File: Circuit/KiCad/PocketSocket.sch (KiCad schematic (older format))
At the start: 0 parts

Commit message: add PowerInput
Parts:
- added C?: 0.1u, symbol C
- added C? (x2): 1u, symbol C
- added P?: CONN_02X25, symbol CONN_02X25
- added P?: I2C_LCD, symbol CONN_01X04
- added U?: CY8CKIT-059_Target, symbol CY8CKIT-059_Target
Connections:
- new net +5V: C?.1, C?.1, C?.2, P?.1 (P1), U?.26 (VDD), U?.52 (VDDIO)
- new net GND: C?.1, C?.2, C?.2, P?.4 (P4), U?.1 (GND), U?.25 (GND), U?.51 (GND)
- new net SCL: P?.2 (P2), U?.42 (P12[0]_I2C_SCL)
- new net SDA: P?.3 (P3), U?.41 (P12[1]_I2C_SDA)
- no-connect marks 0 -> 12

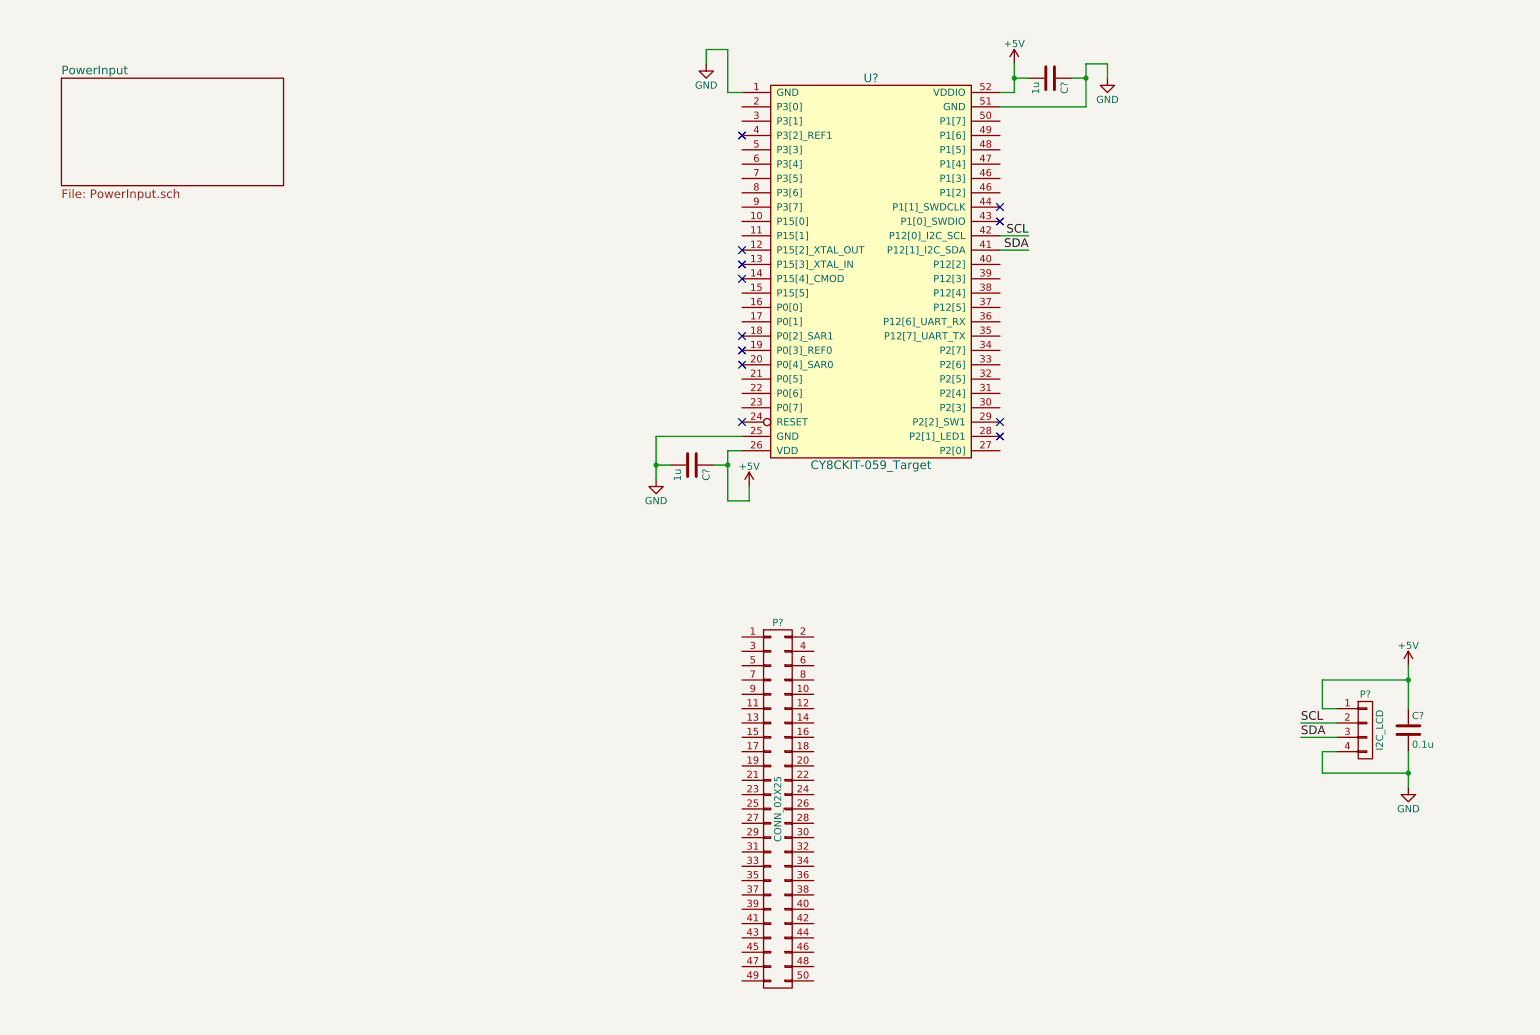
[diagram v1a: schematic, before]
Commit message: add LED driver
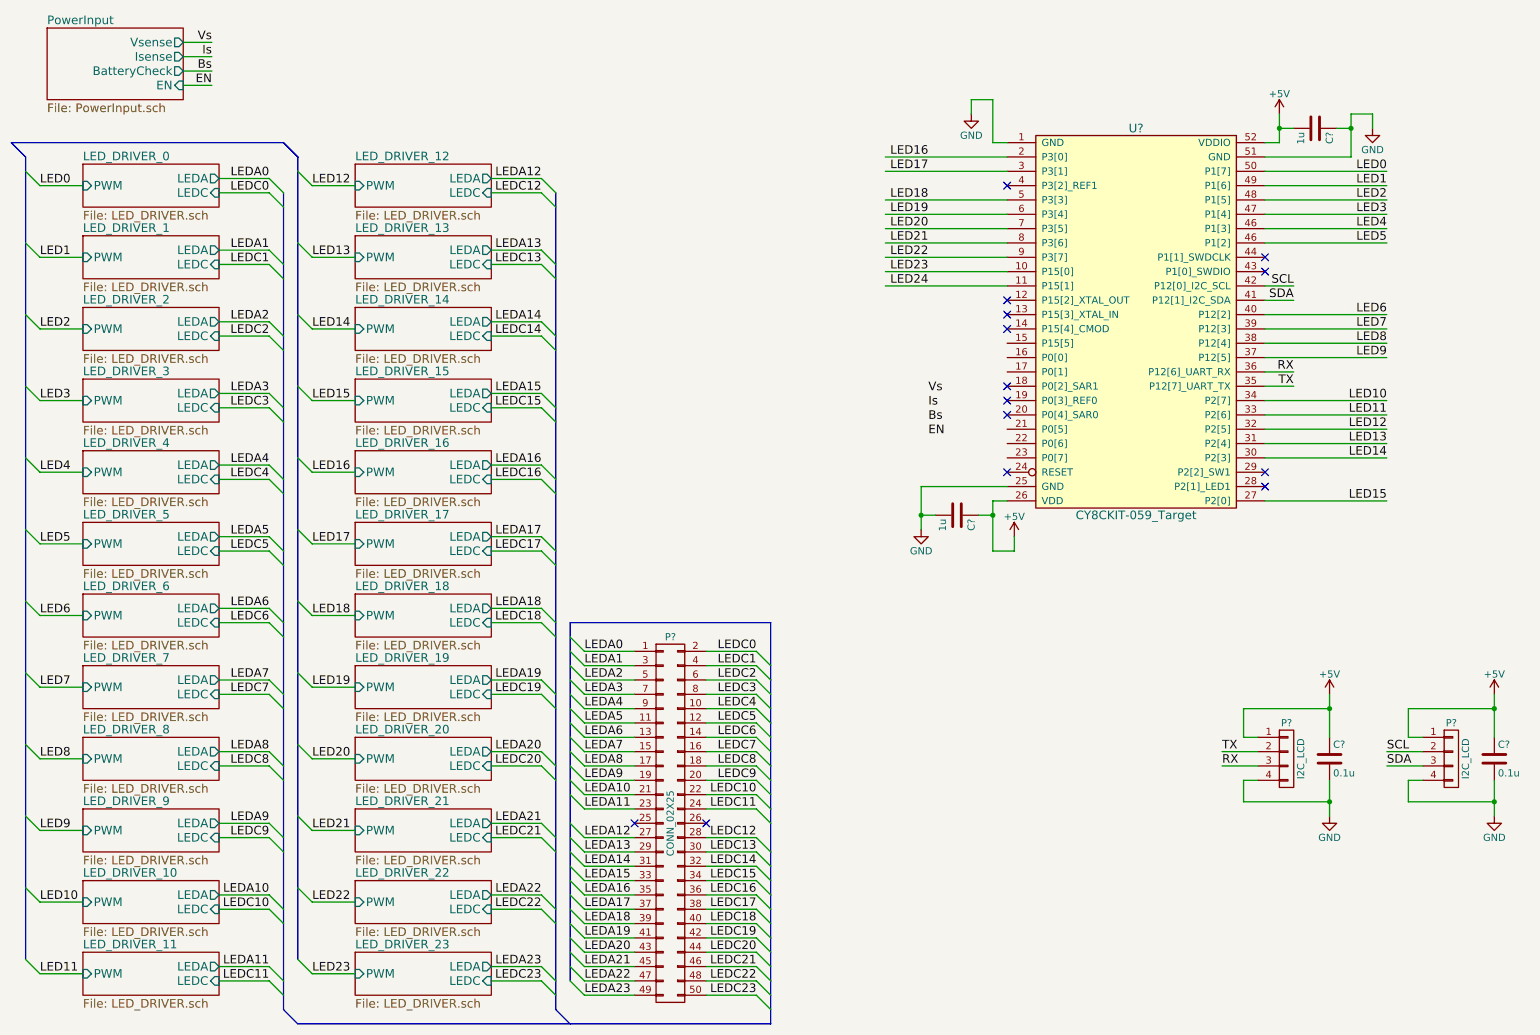
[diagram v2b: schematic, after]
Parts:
- added C?: 0.1u, symbol C
- added P?: I2C_LCD, symbol CONN_01X04
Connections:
- net labels added: Bs, EN, Is, LED0, LED1, LED10, LED11, LED12, LED13, LED14, LED15, LED16, LED17, LED18, LED19, LED2, LED20, LED21, LED22, LED23, LED24, LED3, LED4, LED5, LED6, LED7, LED8, LED9, LEDA0, LEDA1, LEDA10, LEDA11, LEDA12, LEDA13, LEDA14, LEDA15, LEDA16, LEDA17, LEDA18, LEDA19, LEDA2, LEDA20, LEDA21, LEDA22, LEDA23, LEDA3, LEDA4, LEDA5, LEDA6, LEDA7, LEDA8, LEDA9, LEDC0, LEDC1, LEDC10, LEDC11, LEDC12, LEDC13, LEDC14, LEDC15, LEDC16, LEDC17, LEDC18, LEDC19, LEDC2, LEDC20, LEDC21, LEDC22, LEDC23, LEDC3, LEDC4, LEDC5, LEDC6, LEDC7, LEDC8, LEDC9, RX, TX, Vs
- wire segments 32 -> 193
- no-connect marks 12 -> 14
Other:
- moved on the sheet: C?, P?, U?

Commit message: EeSchema settled
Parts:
- added C1, C2: 12p, Capacitors_SMD:C_1206_HandSoldering, symbol C
- added Y1: 24.576M, Crystals:Crystal_HC49-SD_SMD, symbol Crystal
- added Y2: 32.768k, Crystals:Crystal_Round_Horizontal_2mm, symbol Crystal
- C3, C6: renamed from C?; footprint (none) -> Capacitors_ThroughHole:C_Disc_D6_P5
- C4, C5: renamed from C?; value 0.1u -> 1u; footprint (none) -> Capacitors_ThroughHole:C_Disc_D6_P5
- P2: renamed from P?; value I2C_LCD -> UART; footprint (none) -> Connect:bornier4
- P3: renamed from P?; value I2C_LCD -> I2C; footprint (none) -> Connect:bornier4
- gave numbers to parts that had none: 2
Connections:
- net labels removed: LED24
- wire segments 193 -> 222
- no-connect marks 14 -> 10
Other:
- moved on the sheet: C3, C4, C5, C6, P1, P2, P3, U1
